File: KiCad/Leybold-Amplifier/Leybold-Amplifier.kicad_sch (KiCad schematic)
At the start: 40 parts, among them K1 19V, Q1 IRF740, U1 TL497

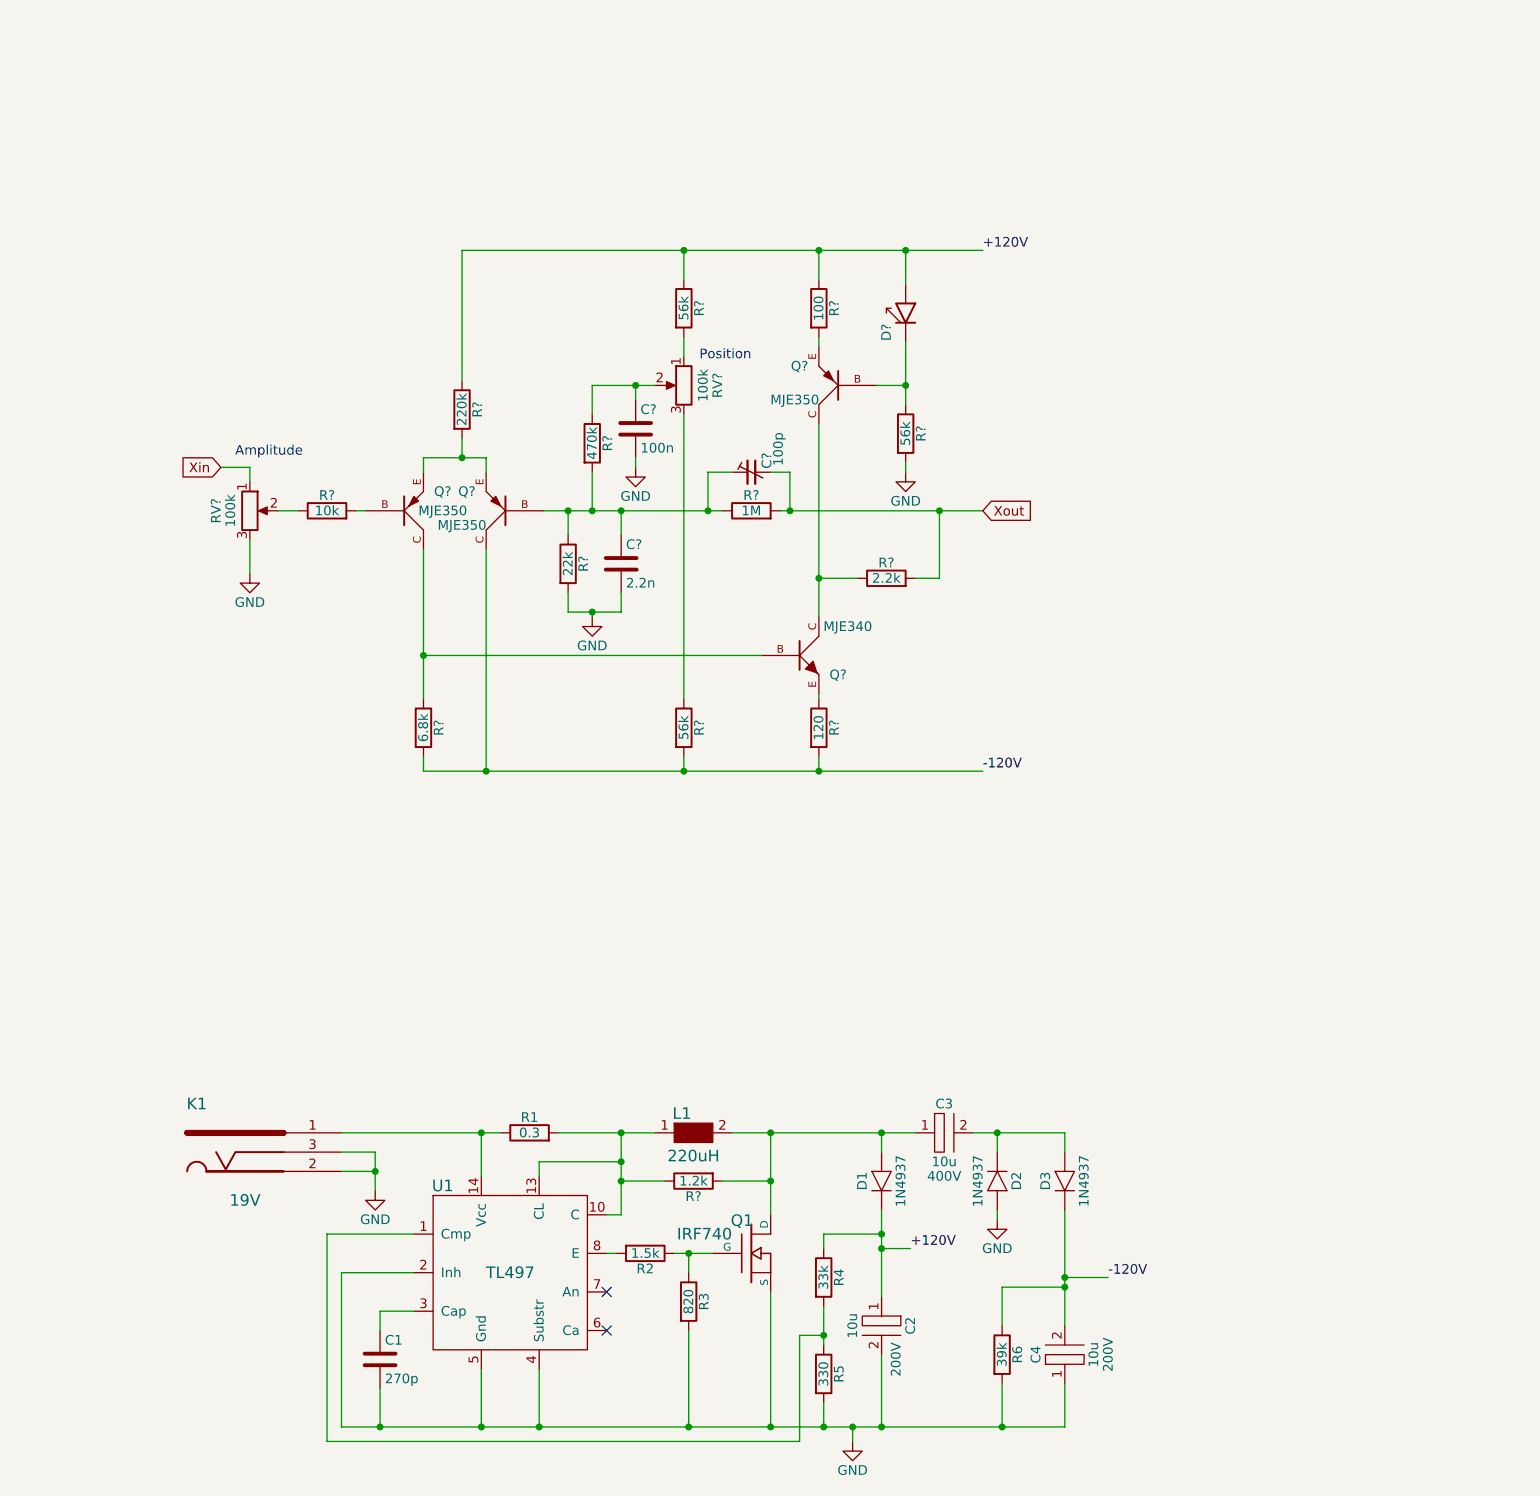
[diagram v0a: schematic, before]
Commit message: Update lightgun LED, add HV, fixes
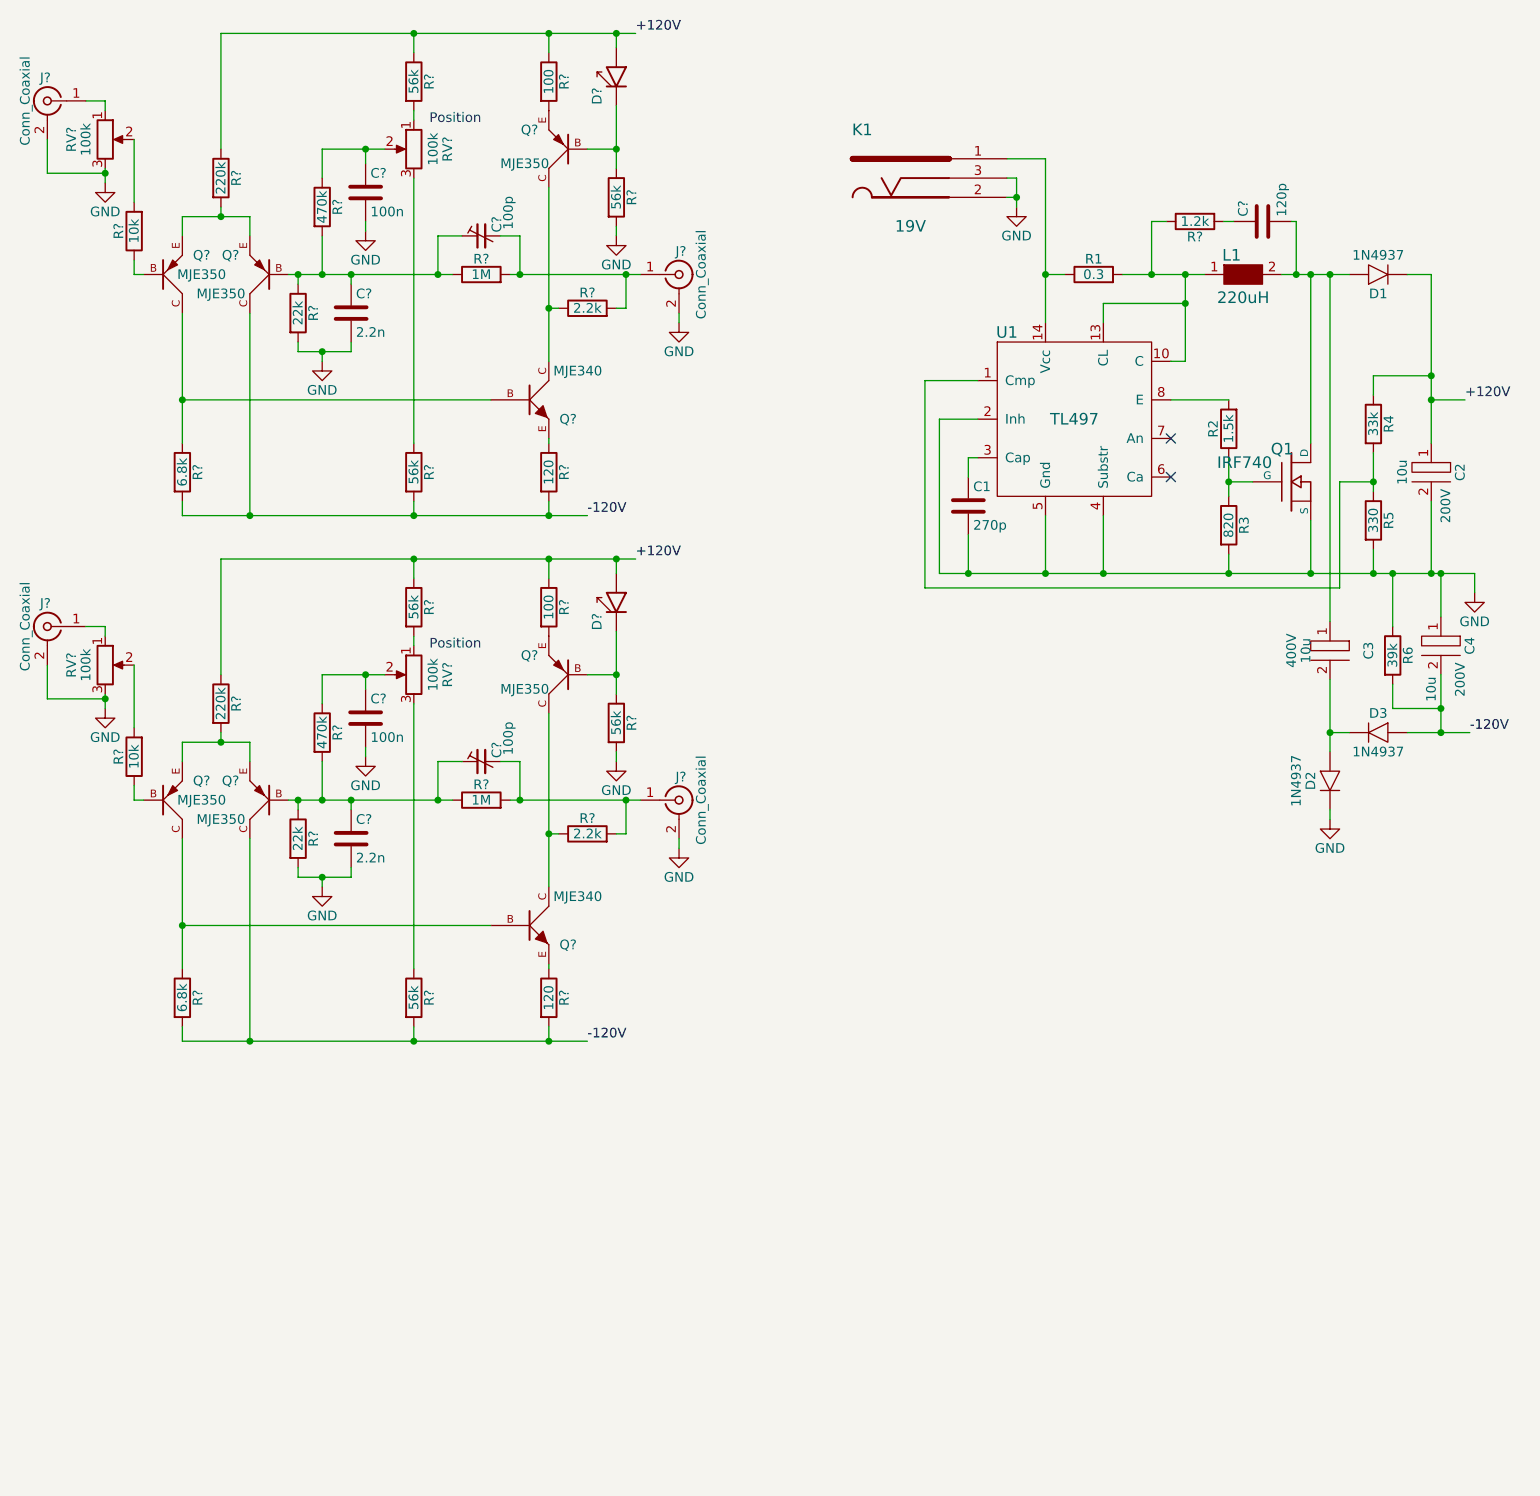
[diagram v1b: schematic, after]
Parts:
- removed Q?: MJE350, symbol rg:BC307
- added C?: 2.2n, symbol Device:C
- added C?: 120p, symbol Device:C
- added C?: 100n, symbol Device:C
- added C?: 100p, symbol Device:C_Trim_Small
- added D?: LED, symbol rg:LED
- added J? (x4): Conn_Coaxial, symbol Connector:Conn_Coaxial
- added Q? (x4): MJE350, symbol rg:BC307
- added Q?: MJE340, TO92-EBC, symbol rg:BC237
- added R?: 1M, symbol Device:R
- added R? (x3): 56k, symbol Device:R
- added R?: 6.8k, symbol Device:R
- added R?: 100, symbol Device:R
- added R?: 10k, symbol Device:R
- added R?: 470k, symbol Device:R
- added R?: 22k, symbol Device:R
- added R?: 120, symbol Device:R
- added R?: 2.2k, symbol Device:R
- added R?: 220k, symbol Device:R
- added RV? (x2): 100k, symbol Device:R_Potentiometer
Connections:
- net +120V: now also D?.A, R?.1, R?.1, R?.1
- net -120V: now also D3.2 (A), R6.2, Q?.C, Q?.C, R?.2, R?.2, R?.2; no longer D3.1 (K), R6.1
- net GND: now also D2.1 (K), R6.1, C?.2, C?.2, J?.2 (Ext), J?.2 (Ext), J?.2 (Ext), J?.2 (Ext), R?.2, R?.2, RV?.3; no longer D2.2 (A), R6.2
- net at Q?.B: now also R?.1; no longer R?.2
- net at Q?.E, R?.2: now also Q?.E
- net at C?.1, C?.1, R?.1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: now also Q?.B
- net at C3.1, D1.2 (A), L1.2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: now also C?.2; no longer R?.2
- net at RV?.2: now also R?.2; no longer R?.1
- net Xin: no longer names the net of RV?.1
- net Xin: now also J?.1 (In)
- net Xout: no longer names the net of C?.2, R?.2, R?.2
- net Xout: now also J?.1 (In)
- new net: R?.2, RV?.1
- new net: C?.1, R?.1, RV?.2
- new net: R?.1, RV?.3
- new net: C?.1, C?.1, Q?.B, R?.1, R?.1, R?.2
- new net: C?.2, J?.1 (In), R?.2, R?.2
- new net: D?.K, Q?.B, R?.1
- new net: J?.1 (In), RV?.1
- new net: Q?.B, R?.1
- new net: Q?.B, Q?.C, R?.1
- new net: Q?.E, Q?.E, R?.2
- new net: C?.1, R?.2
- new net: Q?.C, Q?.C, R?.1
- new net: Q?.E, R?.1
- new net: Q?.E, R?.2
- new net: C3.2, D2.2 (A), D3.1 (K)
- new net: R?.2, RV?.2
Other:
- note removed: "Amplitude"
- moved on the sheet: C1, C2, C3, C4, C?, D1, D2, D3, D?, K1, L1, Q1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
